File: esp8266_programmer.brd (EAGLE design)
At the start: 29.2 x 28.9 mm, 24 parts, among them IC2 UA78M05DCY, J1 10118193-0001LF, Q1 12mhz, Q2 ON_SEMICONDUCTOR_BC849BLT1GON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, Q3 ON_SEMICONDUCTOR_BC849BLT1GON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

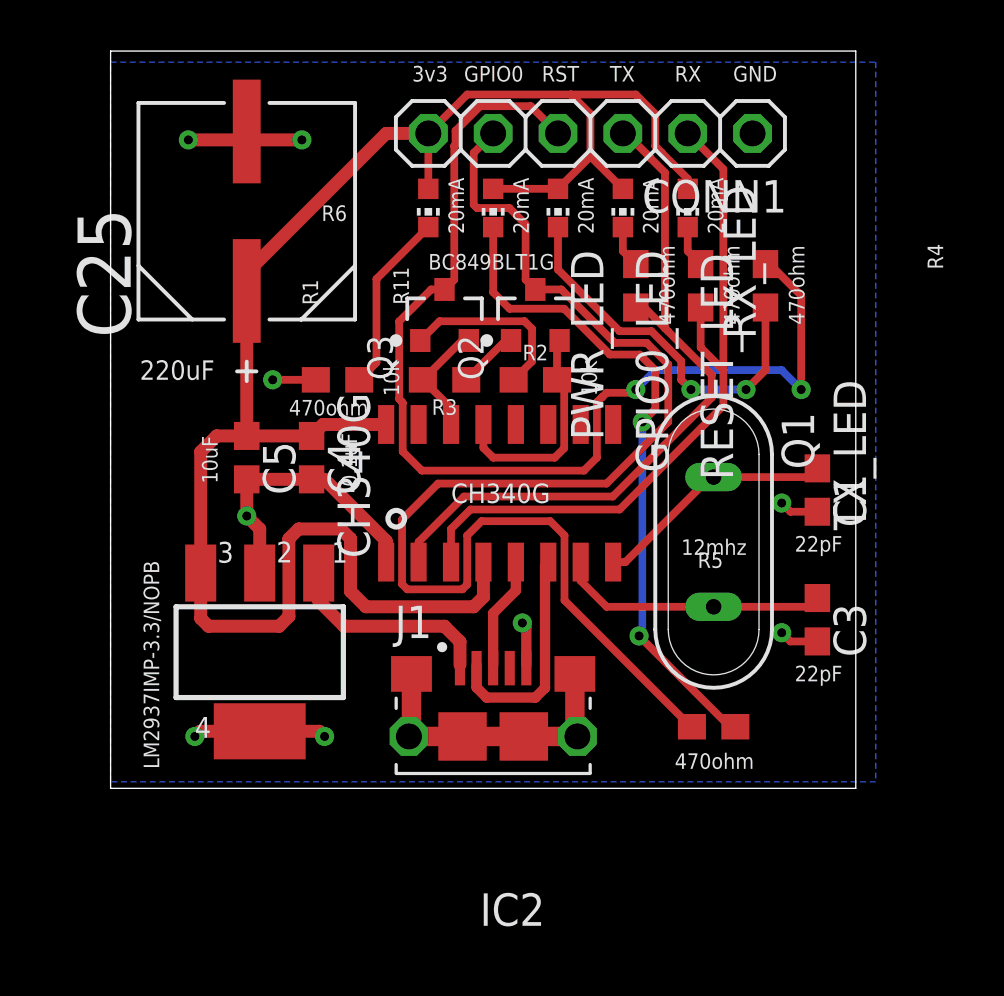
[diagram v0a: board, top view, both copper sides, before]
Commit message: Added library for USB port
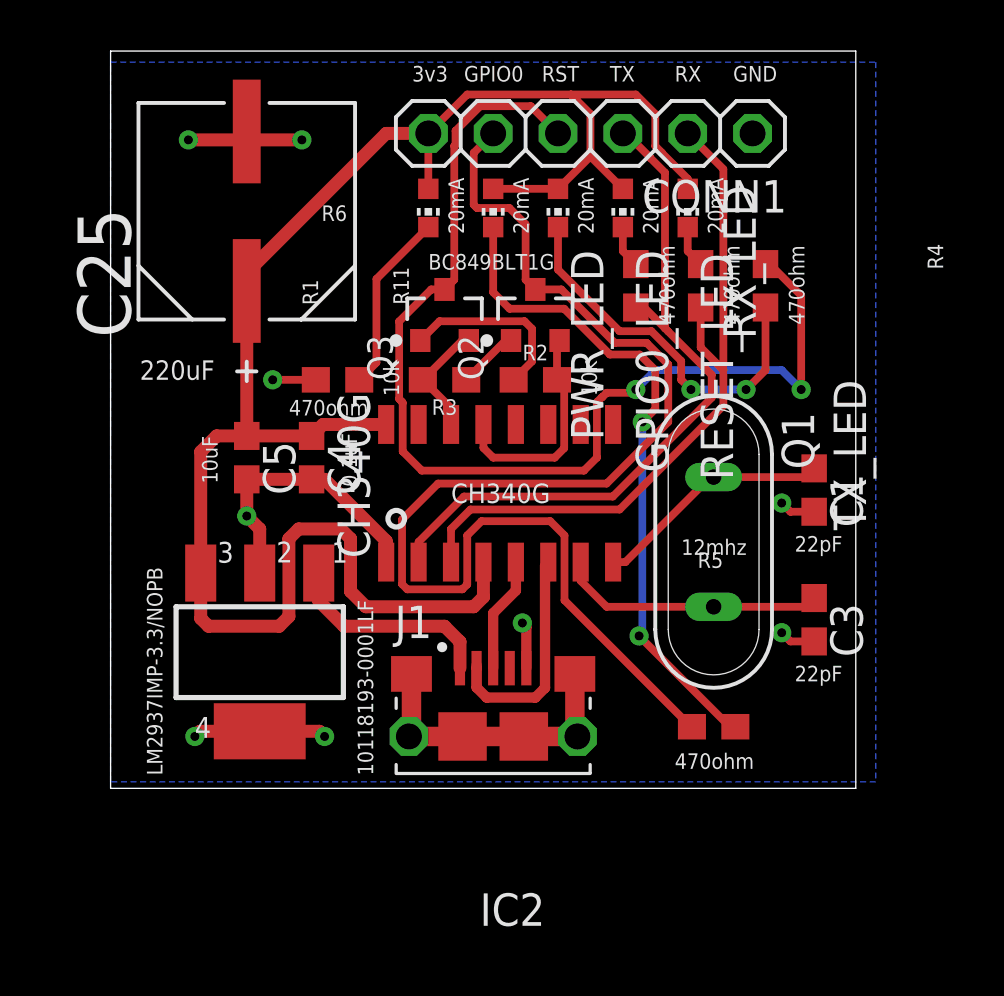
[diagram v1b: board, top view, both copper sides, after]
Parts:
- C25: value 47uF -> 220uF
- moved C1 0.13 mm to (27.6, 11.7)
- moved C3 0.13 mm to (27.6, 6.60)
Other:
- board text added: "10118193-0001LF"
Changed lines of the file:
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@@
 <text x="1.143" y="16.002" size="0.762" layer="21">220uF</text>
 <text x="13.335" y="11.176" size="0.762" layer="21">CH340G</text>
-<text x="1.905" y="0.762" size="0.6096" layer="21" rot="R90">LM2937IMP-3.3/NOPB</text>
+<text x="2.032" y="0.508" size="0.6096" layer="21" rot="R90">LM2937IMP-3.3/NOPB</text>
 <text x="24.003" y="21.717" size="0.6096" layer="21" rot="R90">20mA</text>
 <text x="21.463" y="21.717" size="0.6096" layer="21" rot="R90">20mA</text>
@@
 <text x="22.098" y="27.686" size="0.6096" layer="21">RX</text>
 <text x="24.384" y="27.686" size="0.6096" layer="21">GND</text>
+<text x="10.287" y="0.508" size="0.6096" layer="21" rot="R90">10118193-0001LF</text>
 </plain>
 <attributes>
@@
 </autorouter>
 <elements>
-<element name="C1" library="rcl" library_urn="urn:adsk.eagle:library:334" package="C0603" package3d_urn="urn:adsk.eagle:package:23616/2" value="22pF" x="27.686" y="11.684" smashed="yes" rot="R270">
-<attribute name="NAME" x="28.321" y="12.319" size="1.27" layer="25" rot="R270"/>
-<attribute name="SPICEPREFIX" value="C" x="-10.414" y="-20.066" size="1.778" layer="27" rot="R270" display="off"/>
-<attribute name="VALUE" x="34.417" y="10.541" size="1.27" layer="27" rot="R270"/>
-</element>
-<element name="C25" library="Panasonic-EEEFK_EEEFP" package="CAPAE830X1050N" value="47uF" x="5.334" y="22.606" smashed="yes" rot="R90">
+<element name="C1" library="rcl" library_urn="urn:adsk.eagle:library:334" package="C0603" package3d_urn="urn:adsk.eagle:package:23616/2" value="22pF" x="27.559" y="11.684" smashed="yes" rot="R270">
+<attribute name="NAME" x="28.194" y="12.319" size="1.27" layer="25" rot="R270"/>
+<attribute name="SPICEPREFIX" value="C" x="-10.541" y="-20.066" size="1.778" layer="27" rot="R270" display="off"/>
+<attribute name="VALUE" x="34.29" y="10.541" size="1.27" layer="27" rot="R270"/>
+</element>
+<element name="C25" library="Panasonic-EEEFK_EEEFP" package="CAPAE830X1050N" value="220uF" x="5.334" y="22.606" smashed="yes" rot="R90">
 <attribute name="MPN" value="EEE-FK1C471P" x="12.954" y="41.656" size="1.778" layer="27" rot="R90" display="off"/>
 <attribute name="NAME" x="0.7874" y="17.653" size="2.0828" layer="25" ratio="10" rot="SR90"/>
@@
 <attribute name="VOLTAGERATING" value="16V" x="12.954" y="41.656" size="1.778" layer="27" rot="R90" display="off"/>
 </element>
-<element name="C3" library="rcl" library_urn="urn:adsk.eagle:library:334" package="C0603" package3d_urn="urn:adsk.eagle:package:23616/2" value="22pF" x="27.686" y="6.604" smashed="yes" rot="R270">
-<attribute name="NAME" x="28.321" y="7.239" size="1.27" layer="25" rot="R270"/>
-<attribute name="SPICEPREFIX" value="C" x="-10.414" y="-31.496" size="1.778" layer="27" rot="R270" display="off"/>
-<attribute name="VALUE" x="34.417" y="5.207" size="1.27" layer="27" rot="R270"/>
+<element name="C3" library="rcl" library_urn="urn:adsk.eagle:library:334" package="C0603" package3d_urn="urn:adsk.eagle:package:23616/2" value="22pF" x="27.559" y="6.604" smashed="yes" rot="R270">
+<attribute name="NAME" x="28.194" y="7.239" size="1.27" layer="25" rot="R270"/>
+<attribute name="SPICEPREFIX" value="C" x="-10.541" y="-31.496" size="1.778" layer="27" rot="R270" display="off"/>
+<attribute name="VALUE" x="34.29" y="5.207" size="1.27" layer="27" rot="R270"/>
 </element>
 <element name="C4" library="rcl" library_urn="urn:adsk.eagle:library:334" package="C0603" package3d_urn="urn:adsk.eagle:package:23616/2" value="0.1uF" x="7.874" y="12.954" smashed="yes" rot="R270">
@@
 <wire x1="15.875" y1="7.747" x2="15.875" y2="8.862" width="0.4064" layer="1"/>
 <wire x1="15.875" y1="7.747" x2="14.986" y2="6.858" width="0.4064" layer="1"/>
-<wire x1="14.986" y1="6.858" x2="14.986" y2="4.834" width="0.4064" layer="1"/>
-<wire x1="14.986" y1="4.834" x2="14.986" y2="4.707" width="0" layer="19" extent="1-1"/>
+<wire x1="14.986" y1="6.858" x2="14.986" y2="4.707" width="0.4064" layer="1"/>
 </signal>
 <signal name="D-">
@@
 <wire x1="17.018" y1="8.735" x2="17.145" y2="8.862" width="0.3048" layer="1"/>
 <wire x1="14.732" y1="3.556" x2="16.637" y2="3.556" width="0.4064" layer="1"/>
-<wire x1="14.336" y1="4.834" x2="14.336" y2="3.952" width="0.4064" layer="1"/>
+<wire x1="14.336" y1="4.834" x2="14.336" y2="4.707" width="0.4064" layer="1"/>
 <wire x1="14.336" y1="3.952" x2="14.732" y2="3.556" width="0.4064" layer="1"/>
-<wire x1="14.336" y1="4.834" x2="14.336" y2="4.707" width="0" layer="19" extent="1-1"/>
+<wire x1="14.336" y1="4.707" x2="14.336" y2="3.952" width="0.4064" layer="1"/>
 </signal>
 <signal name="CRYSTALIN">
@@
 <wire x1="19.431" y1="7.112" x2="23.622" y2="7.112" width="0.3048" layer="1"/>
 <wire x1="18.415" y1="8.128" x2="19.431" y2="7.112" width="0.3048" layer="1"/>
-<wire x1="23.622" y1="7.112" x2="27.344" y2="7.112" width="0.3048" layer="1"/>
-<wire x1="27.344" y1="7.112" x2="27.686" y2="7.454" width="0.3048" layer="1"/>
+<wire x1="23.622" y1="7.112" x2="27.217" y2="7.112" width="0.3048" layer="1"/>
+<wire x1="27.217" y1="7.112" x2="27.559" y2="7.454" width="0.3048" layer="1"/>
 </signal>
 <signal name="CRYSTALOUT">
@@
 <wire x1="23.495" y1="12.192" x2="20.165" y2="8.862" width="0.3048" layer="1"/>
 <wire x1="19.685" y1="8.862" x2="20.165" y2="8.862" width="0.3048" layer="1"/>
-<wire x1="27.344" y1="12.192" x2="27.686" y2="12.534" width="0.3048" layer="1"/>
-<wire x1="23.622" y1="12.192" x2="27.344" y2="12.192" width="0.3048" layer="1"/>
+<wire x1="27.217" y1="12.192" x2="27.559" y2="12.534" width="0.3048" layer="1"/>
+<wire x1="23.622" y1="12.192" x2="27.217" y2="12.192" width="0.3048" layer="1"/>
 </signal>
 <signal name="GND">
@@
 <via x="16.129" y="6.477" extent="1-16" drill="0.35"/>
 <wire x1="13.786" y1="2.032" x2="16.186" y2="2.032" width="0.762" layer="1"/>
-<wire x1="18.286" y1="4.509" x2="18.186" y2="4.609" width="0.762" layer="1"/>
-<wire x1="16.129" y1="6.477" x2="16.286" y2="6.32" width="0.4064" layer="1"/>
-<wire x1="16.286" y1="6.32" x2="16.286" y2="4.834" width="0.4064" layer="1"/>
 <wire x1="8.04" y1="16.002" x2="6.35" y2="16.002" width="0.3048" layer="1"/>
 <via x="6.35" y="16.002" extent="1-16" drill="0.35"/>
 <via x="26.289" y="6.096" extent="1-16" drill="0.35"/>
-<wire x1="27.686" y1="10.834" x2="26.631" y2="10.834" width="0.3048" layer="1"/>
+<wire x1="27.559" y1="10.834" x2="26.631" y2="10.834" width="0.3048" layer="1"/>
 <wire x1="26.631" y1="10.834" x2="26.289" y2="11.176" width="0.3048" layer="1"/>
-<wire x1="27.686" y1="5.754" x2="26.631" y2="5.754" width="0.3048" layer="1"/>
+<wire x1="27.559" y1="5.754" x2="26.631" y2="5.754" width="0.3048" layer="1"/>
 <wire x1="26.631" y1="5.754" x2="26.289" y2="6.096" width="0.3048" layer="1"/>
 <wire x1="11.786" y1="4.482" x2="11.786" y2="2.132" width="0.762" layer="1"/>
@@
 <wire x1="18.186" y1="4.482" x2="18.186" y2="2.132" width="0.762" layer="1"/>
 <wire x1="18.186" y1="2.132" x2="18.286" y2="2.032" width="0.762" layer="1"/>
-<wire x1="18.186" y1="4.482" x2="18.286" y2="4.509" width="0" layer="19" extent="1-1"/>
-<wire x1="16.286" y1="4.707" x2="16.286" y2="4.834" width="0" layer="19" extent="1-1"/>
+<wire x1="16.286" y1="4.707" x2="16.286" y2="6.32" width="0.4064" layer="1"/>
+<wire x1="16.286" y1="6.32" x2="16.129" y2="6.477" width="0.4064" layer="1"/>
 </signal>
 <signal name="VCC">
@@
 <contactref element="TX_LED" pad="A"/>
 <contactref element="RX_LED" pad="A"/>
-<wire x1="22.606" y1="23.483" x2="22.606" y2="23.749" width="0.3048" layer="1"/>
 <wire x1="20.574" y1="27.178" x2="18.034" y2="27.178" width="0.3048" layer="1"/>
 <wire x1="18.034" y1="27.178" x2="13.97" y2="27.178" width="0.3048" layer="1"/>
@@
 <wire x1="5.334" y1="20.193" x2="5.334" y2="19.4818" width="0.508" layer="1"/>
 <wire x1="12.446" y1="23.483" x2="12.446" y2="25.654" width="0.3048" layer="1"/>
-<wire x1="22.606" y1="23.483" x2="22.606" y2="23.876" width="0.3048" layer="1"/>
 <wire x1="21.59691875" y1="24.88508125" x2="21.59691875" y2="24.896671875" width="0.3048" layer="1"/>
 <wire x1="21.59691875" y1="24.896671875" x2="21.336" y2="25.157590625" width="0.3048" layer="1"/>
@@
 <wire x1="21.336" y1="26.416" x2="20.574" y2="27.178" width="0.3048" layer="1"/>
 <wire x1="21.336" y1="25.157590625" x2="21.336" y2="26.416" width="0.3048" layer="1"/>
+<wire x1="22.606" y1="23.483" x2="22.606" y2="23.876" width="0.3048" layer="1"/>
 </signal>
 <signal name="TXFROMMCU">
@@
 <wire x1="13.081" y1="6.35" x2="9.144" y2="6.35" width="0.508" layer="1"/>
 <wire x1="9.144" y1="6.35" x2="8.1534" y2="7.3406" width="0.508" layer="1"/>
-<wire x1="13.686" y1="5.745" x2="13.686" y2="4.834" width="0.508" layer="1"/>
-<wire x1="13.686" y1="4.834" x2="13.686" y2="4.707" width="0" layer="19" extent="1-1"/>
+<wire x1="13.686" y1="5.745" x2="13.686" y2="4.707" width="0.508" layer="1"/>
 </signal>
 <signal name="STATUSTOLED">
@@
 <wire x1="24.892" y1="15.621" x2="22.733" y2="15.621" width="0.3048" layer="16"/>
 <via x="24.892" y="15.621" extent="1-16" drill="0.35"/>
-<wire x1="25.996" y1="18.835" x2="25.654" y2="18.835" width="0.3048" layer="1"/>
 <wire x1="22.352" y1="16.002" x2="22.733" y2="15.621" width="0.3048" layer="1"/>
 <wire x1="22.352" y1="16.7408375" x2="21.1858375" y2="17.907" width="0.3048" layer="1"/>
